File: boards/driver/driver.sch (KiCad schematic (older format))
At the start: 0 parts

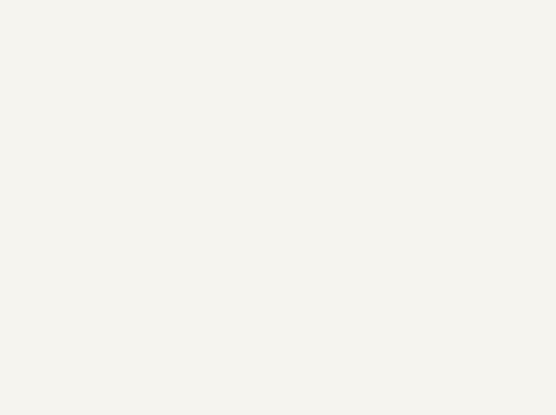
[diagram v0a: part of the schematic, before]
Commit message: Added a sheet containing all of the required current drivers to the interface board
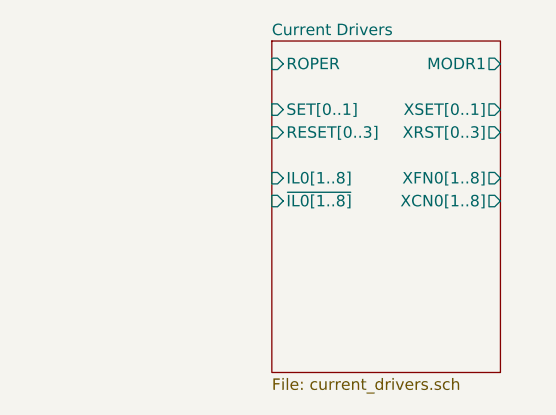
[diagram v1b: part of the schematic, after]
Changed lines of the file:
@@
 $Descr USLedger 17000 11000
 encoding utf-8
-Sheet 1 2
+Sheet 1 3
 Title ""
 Date ""
@@
 F5 "SA[01..16]" O R 5200 1750 50
 $EndSheet
+$Sheet
+S 6650 1500 1000 1450
+U 6183FAE6
+F0 "Current Drivers" 50
+F1 "current_drivers.sch" 50
+F2 "MODR1" O R 7650 1600 50
+F3 "ROPER" I L 6650 1600 50
+F4 "SET[0..1]" I L 6650 1800 50
+F5 "XSET[0..1]" O R 7650 1800 50
+F6 "RESET[0..3]" I L 6650 1900 50
+F7 "XRST[0..3]" O R 7650 1900 50
+F8 "~IL0[1..8]" I L 6650 2200 50
+F9 "IL0[1..8]" I L 6650 2100 50
+F10 "XFN0[1..8]" O R 7650 2100 50
+F11 "XCN0[1..8]" O R 7650 2200 50
+$EndSheet
 $EndSCHEMATC

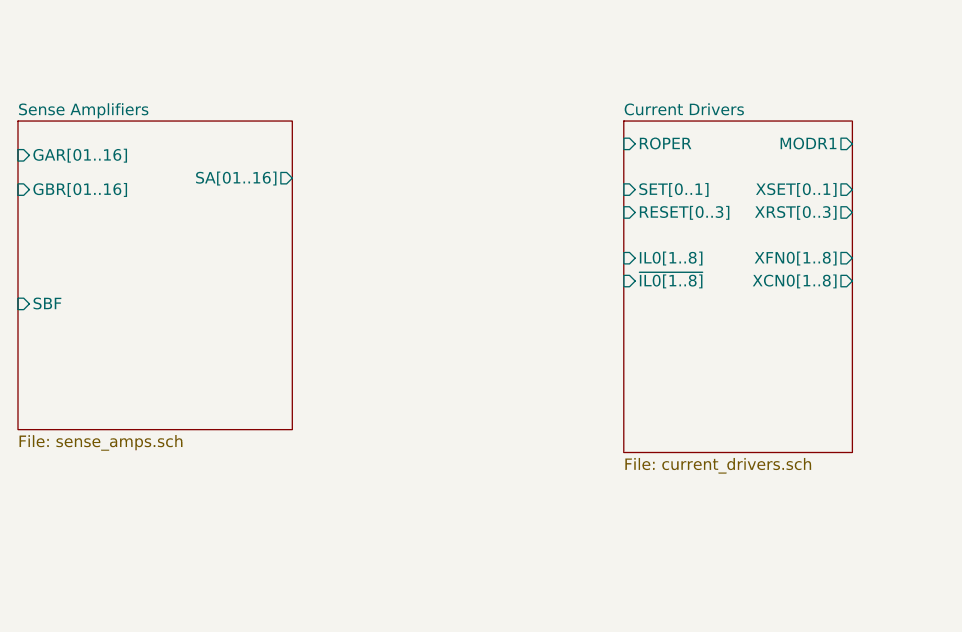
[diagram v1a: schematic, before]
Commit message: Driver board: added strand selection and return circuits
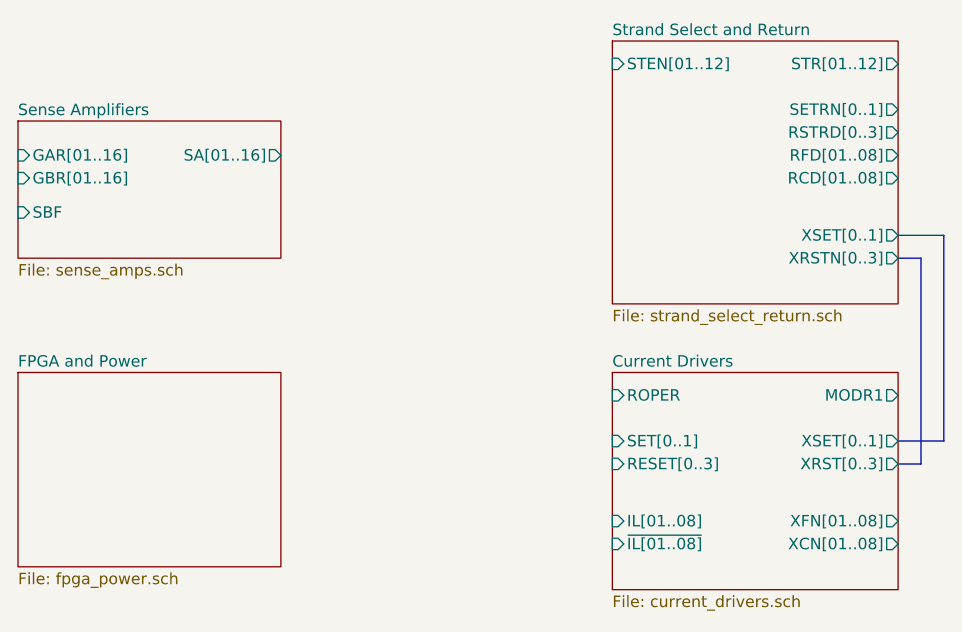
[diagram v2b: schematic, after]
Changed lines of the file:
@@
 $Descr USLedger 17000 11000
 encoding utf-8
-Sheet 1 3
+Sheet 1 4
 Title ""
 Date ""
@@
 $EndDescr
 $Sheet
-S 4000 1500 1200 1350
+S 4000 1500 1150 600
 U 61EC7443
 F0 "Sense Amplifiers" 50
 F1 "sense_amps.sch" 50
-F2 "SBF" I L 4000 2300 50
+F2 "SBF" I L 4000 1900 50
 F3 "GAR[01..16]" I L 4000 1650 50
-F4 "GBR[01..16]" I L 4000 1800 50
-F5 "SA[01..16]" O R 5200 1750 50
+F4 "GBR[01..16]" I L 4000 1750 50
+F5 "SA[01..16]" O R 5150 1650 50
 $EndSheet
 $Sheet
-S 6650 1500 1000 1450
+S 6600 1150 1250 1150
+U 64D2DF1E
+F0 "Strand Select and Return" 50
+F1 "strand_select_return.sch" 50
+F2 "STEN[01..12]" I L 6600 1250 50
+F3 "STR[01..12]" O R 7850 1250 50
+F4 "SETRN[0..1]" O R 7850 1450 50
+F5 "XSET[0..1]" O R 7850 2000 50
+F6 "RSTRD[0..3]" O R 7850 1550 50
+F7 "XRSTN[0..3]" O R 7850 2100 50
+F8 "RFD[01..08]" O R 7850 1650 50
+F9 "RCD[01..08]" O R 7850 1750 50
+$EndSheet
+$Sheet
+S 6600 2600 1250 950
 U 6183FAE6
 F0 "Current Drivers" 50
 F1 "current_drivers.sch" 50
-F2 "MODR1" O R 7650 1600 50
-F3 "ROPER" I L 6650 1600 50
-F4 "SET[0..1]" I L 6650 1800 50
-F5 "XSET[0..1]" O R 7650 1800 50
-F6 "RESET[0..3]" I L 6650 1900 50
-F7 "XRST[0..3]" O R 7650 1900 50
-F8 "~IL0[1..8]" I L 6650 2200 50
-F9 "IL0[1..8]" I L 6650 2100 50
-F10 "XFN0[1..8]" O R 7650 2100 50
-F11 "XCN0[1..8]" O R 7650 2200 50
+F2 "MODR1" O R 7850 2700 50
+F3 "ROPER" I L 6600 2700 50
+F4 "SET[0..1]" I L 6600 2900 50
+F5 "XSET[0..1]" O R 7850 2900 50
+F6 "RESET[0..3]" I L 6600 3000 50
+F7 "XRST[0..3]" O R 7850 3000 50
+F8 "~IL[01..08]" I L 6600 3350 50
+F9 "IL[01..08]" I L 6600 3250 50
+F10 "XFN[01..08]" O R 7850 3250 50
+F11 "XCN[01..08]" O R 7850 3350 50
+$EndSheet
+Wire Bus Line
+	7850 2000 8050 2000
+Wire Bus Line
+	8050 2000 8050 2900
+Wire Bus Line
+	8050 2900 7850 2900
+Wire Bus Line
+	7850 2100 7950 2100
+Wire Bus Line
+	7950 2100 7950 3000
+Wire Bus Line
+	7950 3000 7850 3000
+$Sheet
+S 4000 2600 1150 850
+U 652D8F7B
+F0 "FPGA and Power" 50
+F1 "fpga_power.sch" 50
 $EndSheet
 $EndSCHEMATC

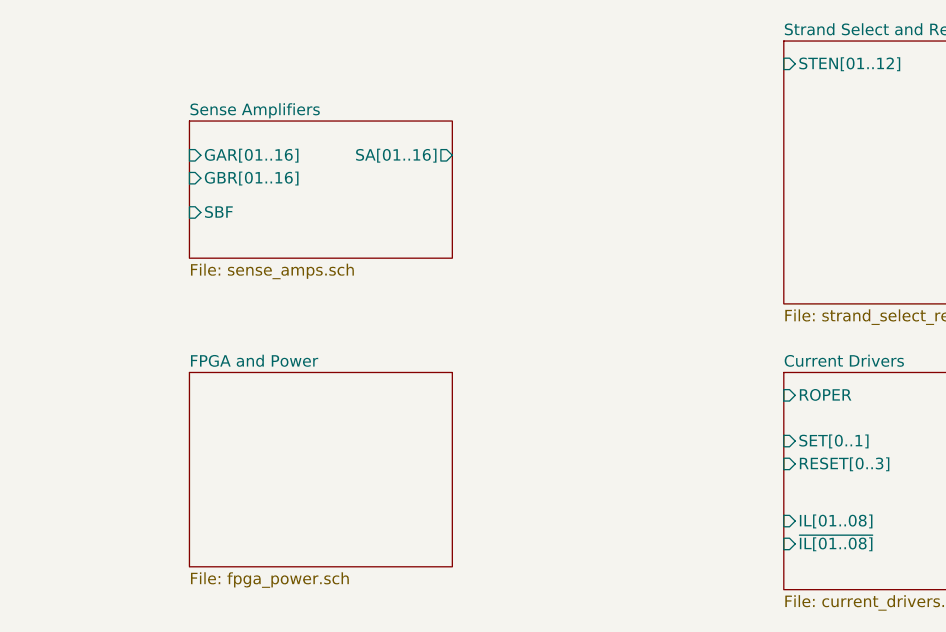
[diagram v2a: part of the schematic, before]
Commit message: Driver board: added a preliminary sheet for the FPGA connector and interfacing circuitry
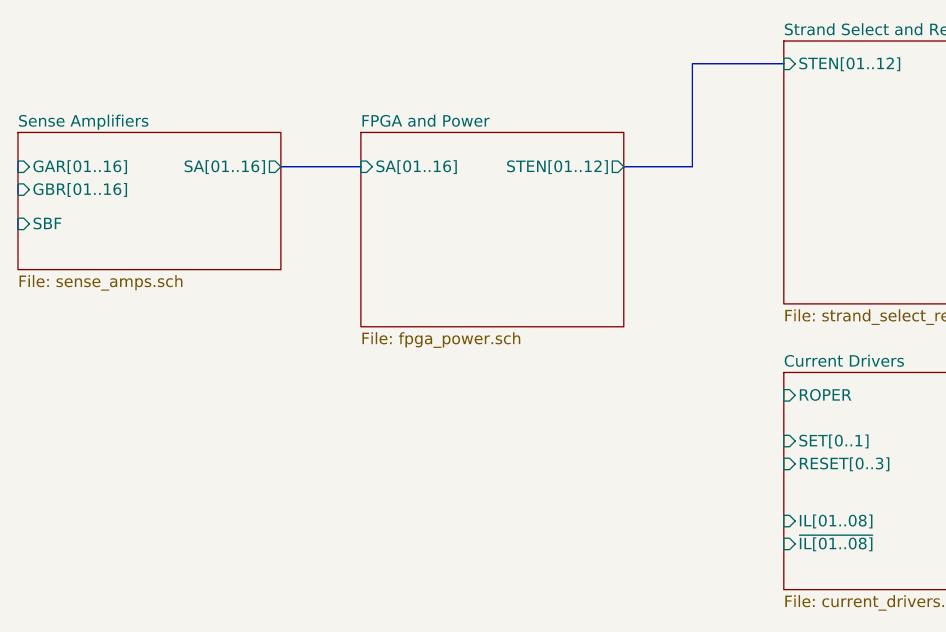
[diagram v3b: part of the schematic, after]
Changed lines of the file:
@@
 $Descr USLedger 17000 11000
 encoding utf-8
-Sheet 1 4
+Sheet 1 5
 Title ""
 Date ""
@@
 $EndDescr
 $Sheet
-S 4000 1500 1150 600
+S 3250 1550 1150 600
 U 61EC7443
 F0 "Sense Amplifiers" 50
 F1 "sense_amps.sch" 50
-F2 "SBF" I L 4000 1900 50
-F3 "GAR[01..16]" I L 4000 1650 50
-F4 "GBR[01..16]" I L 4000 1750 50
-F5 "SA[01..16]" O R 5150 1650 50
+F2 "SBF" I L 3250 1950 50
+F3 "GAR[01..16]" I L 3250 1700 50
+F4 "GBR[01..16]" I L 3250 1800 50
+F5 "SA[01..16]" O R 4400 1700 50
 $EndSheet
 $Sheet
@@
 	7950 3000 7850 3000
 $Sheet
-S 4000 2600 1150 850
+S 4750 1550 1150 850
 U 652D8F7B
 F0 "FPGA and Power" 50
 F1 "fpga_power.sch" 50
+F2 "SA[01..16]" I L 4750 1700 50
+F3 "STEN[01..12]" O R 5900 1700 50
 $EndSheet
+Wire Bus Line
+	4400 1700 4750 1700
+Wire Bus Line
+	5900 1700 6200 1700
+Wire Bus Line
+	6200 1700 6200 1250
+Wire Bus Line
+	6200 1250 6600 1250
 $EndSCHEMATC

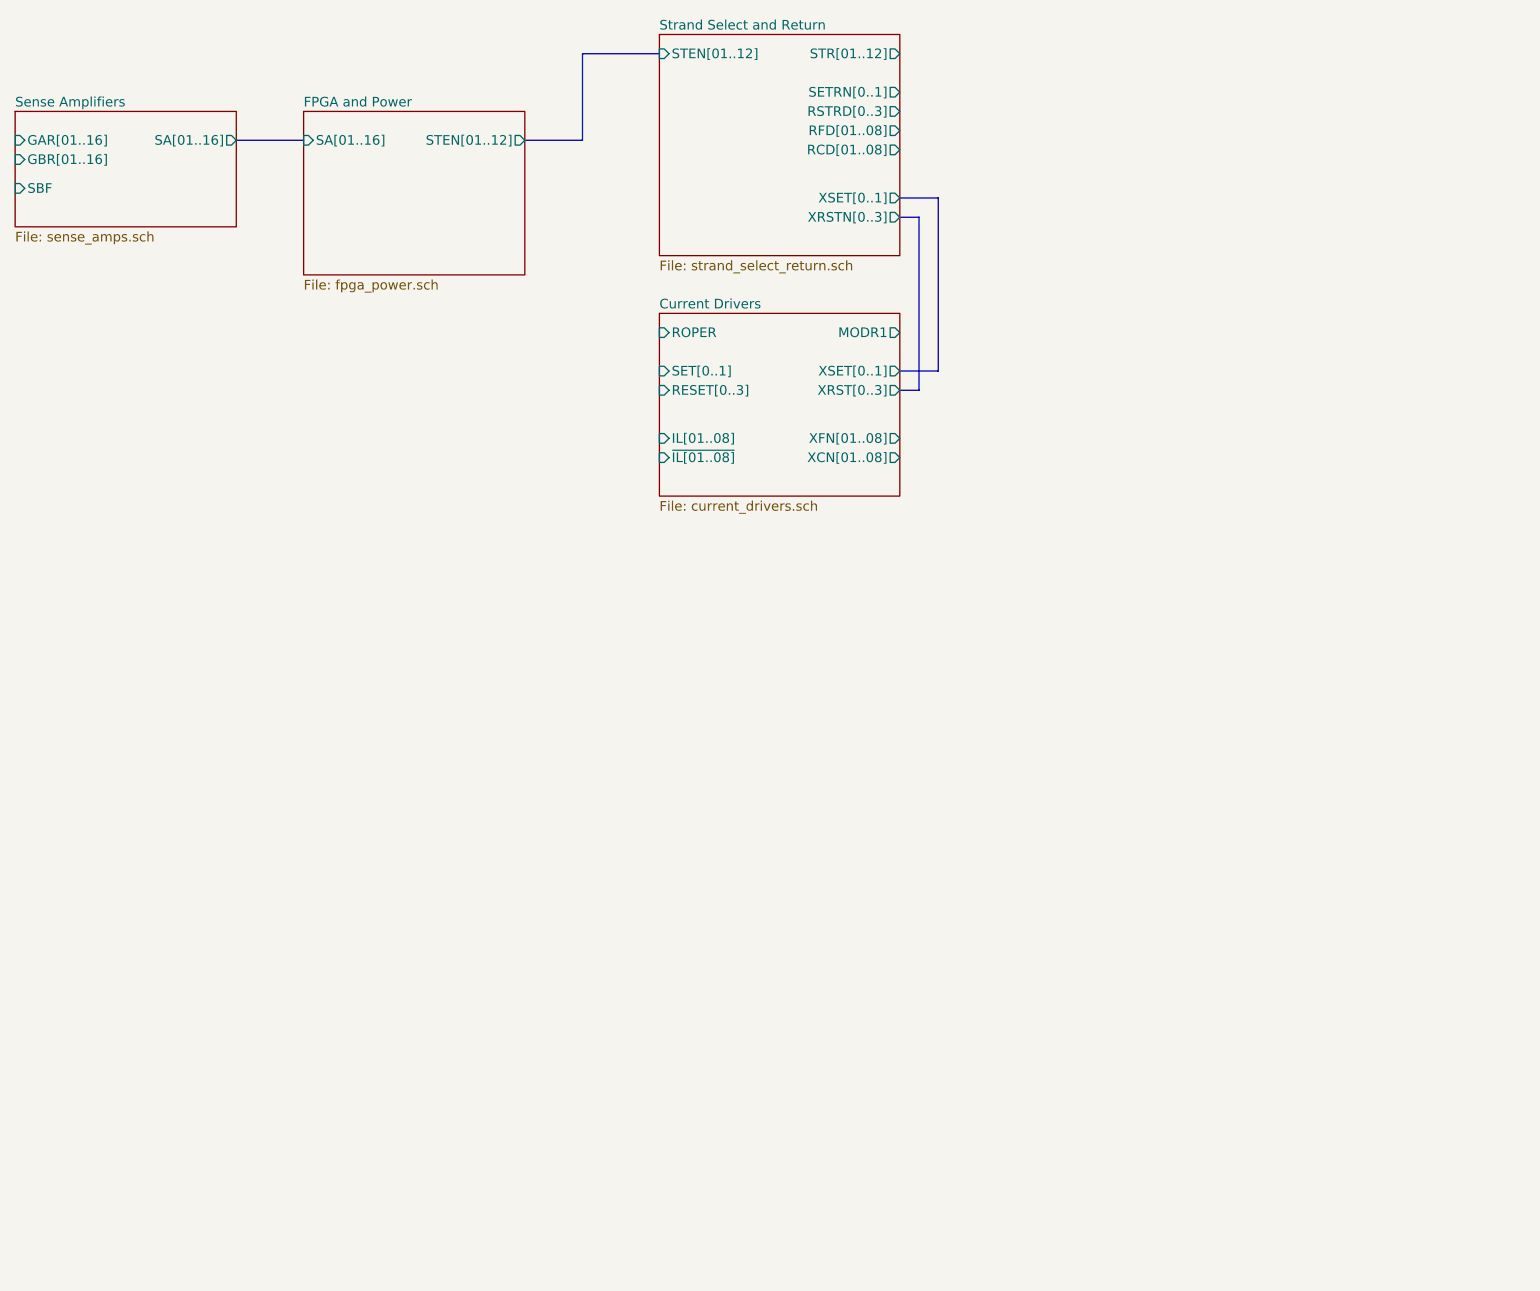
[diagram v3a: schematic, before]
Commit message: Driver boards: filled out all of the FPGA connections. Power circuits to still be defined.
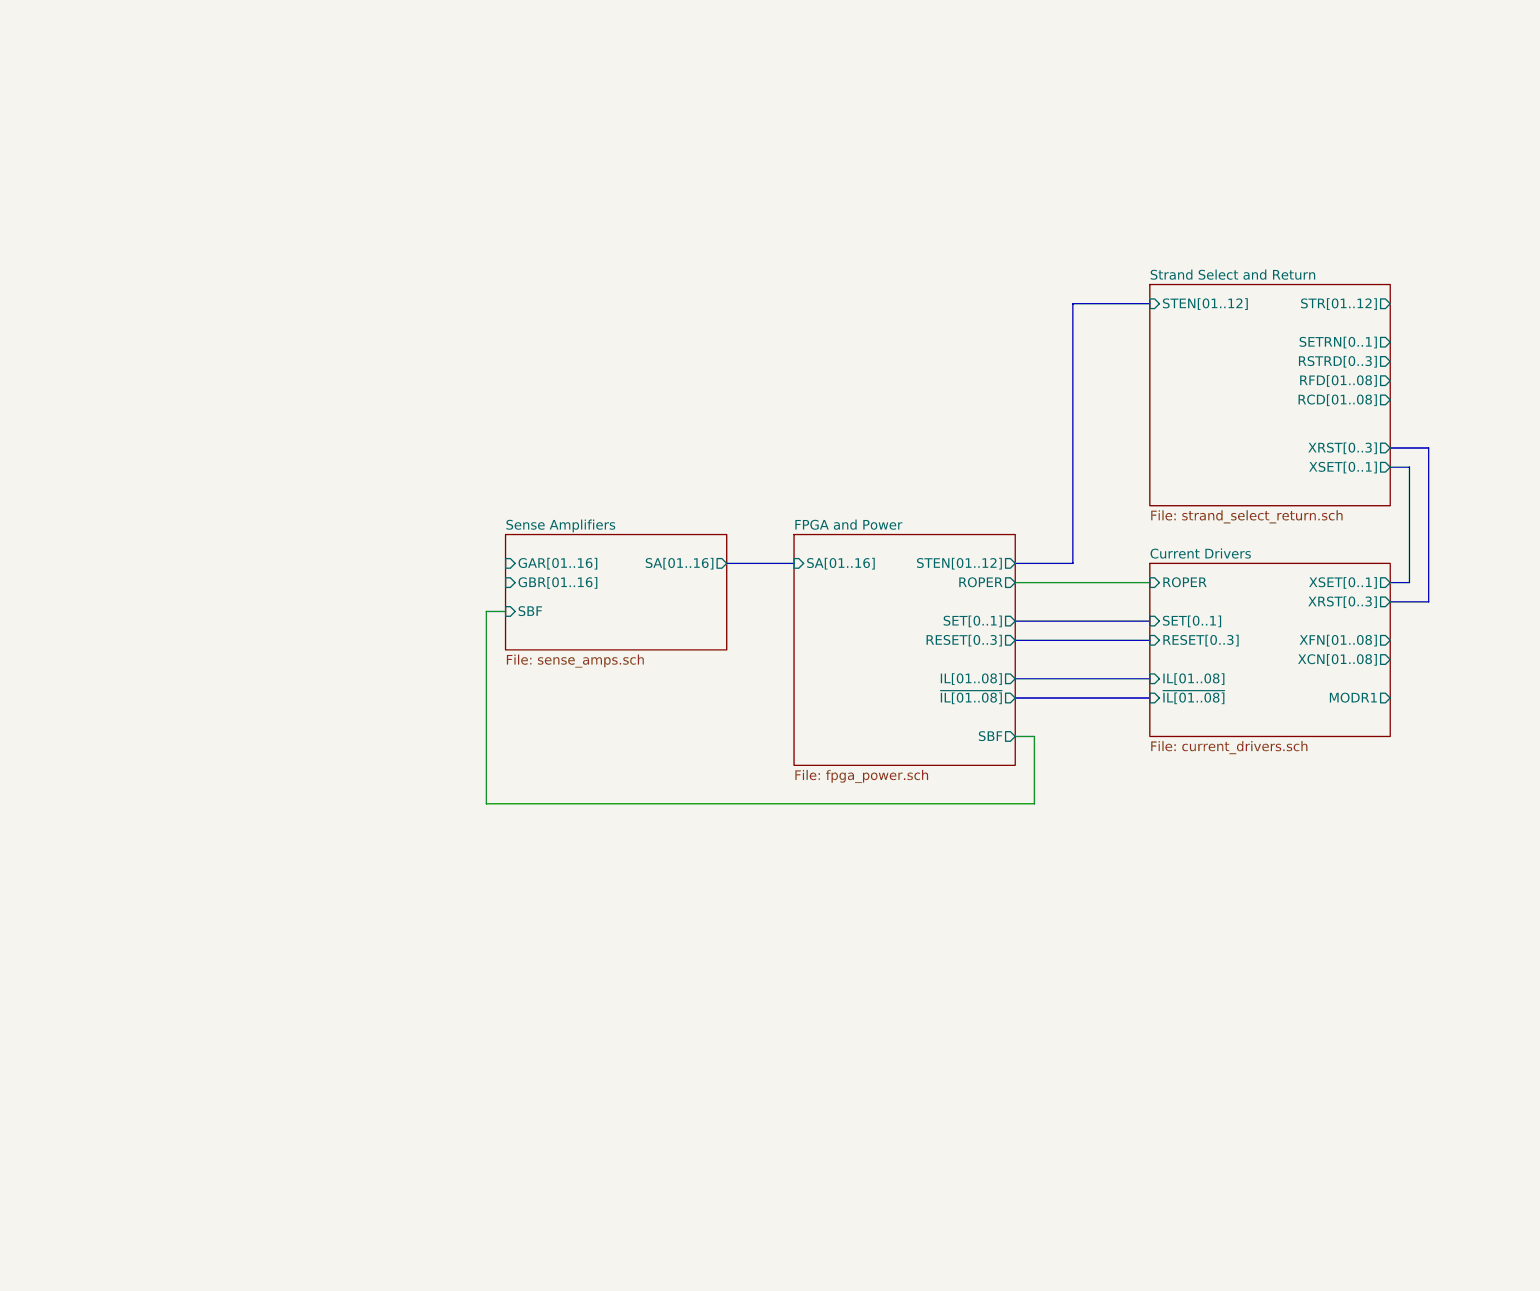
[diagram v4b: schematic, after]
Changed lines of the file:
@@
 $EndDescr
 $Sheet
-S 3250 1550 1150 600
+S 5800 3750 1150 600
 U 61EC7443
 F0 "Sense Amplifiers" 50
 F1 "sense_amps.sch" 50
-F2 "SBF" I L 3250 1950 50
-F3 "GAR[01..16]" I L 3250 1700 50
-F4 "GBR[01..16]" I L 3250 1800 50
-F5 "SA[01..16]" O R 4400 1700 50
+F2 "SBF" I L 5800 4150 50
+F3 "GAR[01..16]" I L 5800 3900 50
+F4 "GBR[01..16]" I L 5800 4000 50
+F5 "SA[01..16]" O R 6950 3900 50
 $EndSheet
 $Sheet
-S 6600 1150 1250 1150
+S 9150 2450 1250 1150
 U 64D2DF1E
 F0 "Strand Select and Return" 50
 F1 "strand_select_return.sch" 50
-F2 "STEN[01..12]" I L 6600 1250 50
-F3 "STR[01..12]" O R 7850 1250 50
-F4 "SETRN[0..1]" O R 7850 1450 50
-F5 "XSET[0..1]" O R 7850 2000 50
-F6 "RSTRD[0..3]" O R 7850 1550 50
-F7 "XRSTN[0..3]" O R 7850 2100 50
-F8 "RFD[01..08]" O R 7850 1650 50
-F9 "RCD[01..08]" O R 7850 1750 50
+F2 "STEN[01..12]" I L 9150 2550 50
+F3 "STR[01..12]" O R 10400 2550 50
+F4 "SETRN[0..1]" O R 10400 2750 50
+F5 "XSET[0..1]" O R 10400 3400 50
+F6 "RSTRD[0..3]" O R 10400 2850 50
+F7 "XRST[0..3]" O R 10400 3300 50
+F8 "RFD[01..08]" O R 10400 2950 50
+F9 "RCD[01..08]" O R 10400 3050 50
 $EndSheet
 $Sheet
-S 6600 2600 1250 950
+S 9150 3900 1250 900
 U 6183FAE6
 F0 "Current Drivers" 50
 F1 "current_drivers.sch" 50
-F2 "MODR1" O R 7850 2700 50
-F3 "ROPER" I L 6600 2700 50
-F4 "SET[0..1]" I L 6600 2900 50
-F5 "XSET[0..1]" O R 7850 2900 50
-F6 "RESET[0..3]" I L 6600 3000 50
-F7 "XRST[0..3]" O R 7850 3000 50
-F8 "~IL[01..08]" I L 6600 3350 50
-F9 "IL[01..08]" I L 6600 3250 50
-F10 "XFN[01..08]" O R 7850 3250 50
-F11 "XCN[01..08]" O R 7850 3350 50
+F2 "MODR1" O R 10400 4600 50
+F3 "ROPER" I L 9150 4000 50
+F4 "SET[0..1]" I L 9150 4200 50
+F5 "XSET[0..1]" O R 10400 4000 50
+F6 "RESET[0..3]" I L 9150 4300 50
+F7 "XRST[0..3]" O R 10400 4100 50
+F8 "~IL[01..08]" I L 9150 4600 50
+F9 "IL[01..08]" I L 9150 4500 50
+F10 "XFN[01..08]" O R 10400 4300 50
+F11 "XCN[01..08]" O R 10400 4400 50
 $EndSheet
 Wire Bus Line
-	7850 2000 8050 2000
+	10400 3300 10600 3300
 Wire Bus Line
-	8050 2000 8050 2900
+	10400 3400 10500 3400
 Wire Bus Line
-	8050 2900 7850 2900
+	10500 3400 10500 4000
 Wire Bus Line
-	7850 2100 7950 2100
-Wire Bus Line
-	7950 2100 7950 3000
-Wire Bus Line
-	7950 3000 7850 3000
+	10500 4000 10400 4000
 $Sheet
-S 4750 1550 1150 850
+S 7300 3750 1150 1200
 U 652D8F7B
 F0 "FPGA and Power" 50
 F1 "fpga_power.sch" 50
-F2 "SA[01..16]" I L 4750 1700 50
-F3 "STEN[01..12]" O R 5900 1700 50
+F2 "SA[01..16]" I L 7300 3900 50
+F3 "STEN[01..12]" O R 8450 3900 50
+F4 "SET[0..1]" O R 8450 4200 50
+F5 "RESET[0..3]" O R 8450 4300 50
+F6 "IL[01..08]" O R 8450 4500 50
+F7 "~IL[01..08]" O R 8450 4600 50
+F8 "ROPER" O R 8450 4000 50
+F9 "SBF" O R 8450 4800 50
 $EndSheet
 Wire Bus Line
-	4400 1700 4750 1700
+	6950 3900 7300 3900
 Wire Bus Line
-	5900 1700 6200 1700
+	8450 3900 8750 3900
 Wire Bus Line
-	6200 1700 6200 1250
+	8750 3900 8750 2550
 Wire Bus Line
-	6200 1250 6600 1250
+	8750 2550 9150 2550
+Wire Wire Line
+	8450 4000 9150 4000
+Wire Bus Line
+	8450 4200 9150 4200
+Wire Bus Line
+	8450 4300 9150 4300
+Wire Bus Line
+	8450 4500 9150 4500
+Wire Bus Line
+	9150 4600 8450 4600
+Wire Wire Line
+	8450 4800 8550 4800
+Wire Wire Line
+	8550 4800 8550 5150
+Wire Wire Line
+	8550 5150 5700 5150
+Wire Wire Line
+	5700 5150 5700 4150
+Wire Wire Line
+	5700 4150 5800 4150
+Wire Bus Line
+	10400 4100 10600 4100
+Wire Bus Line
+	10600 3300 10600 4100
 $EndSCHEMATC
